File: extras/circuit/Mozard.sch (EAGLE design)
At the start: 43 parts, among them J4 Headphone/Line Out, U2 LM386

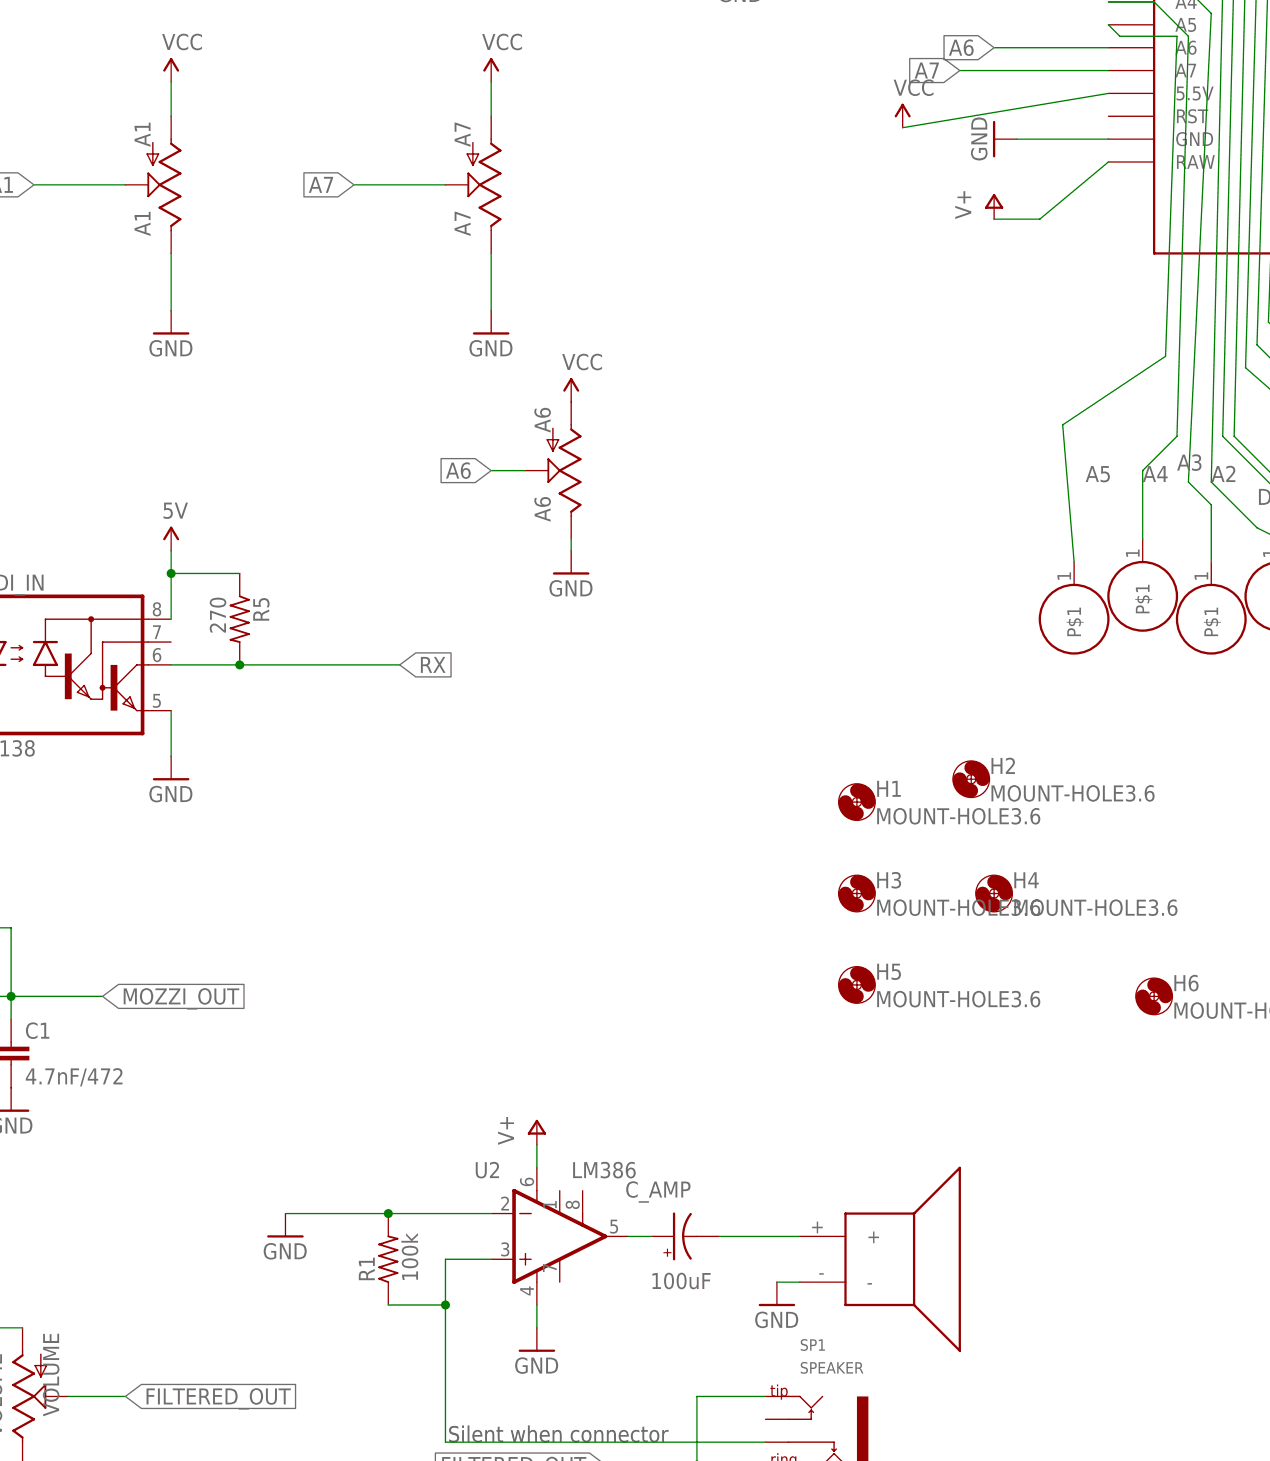
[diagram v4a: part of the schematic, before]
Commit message: Added MIDI
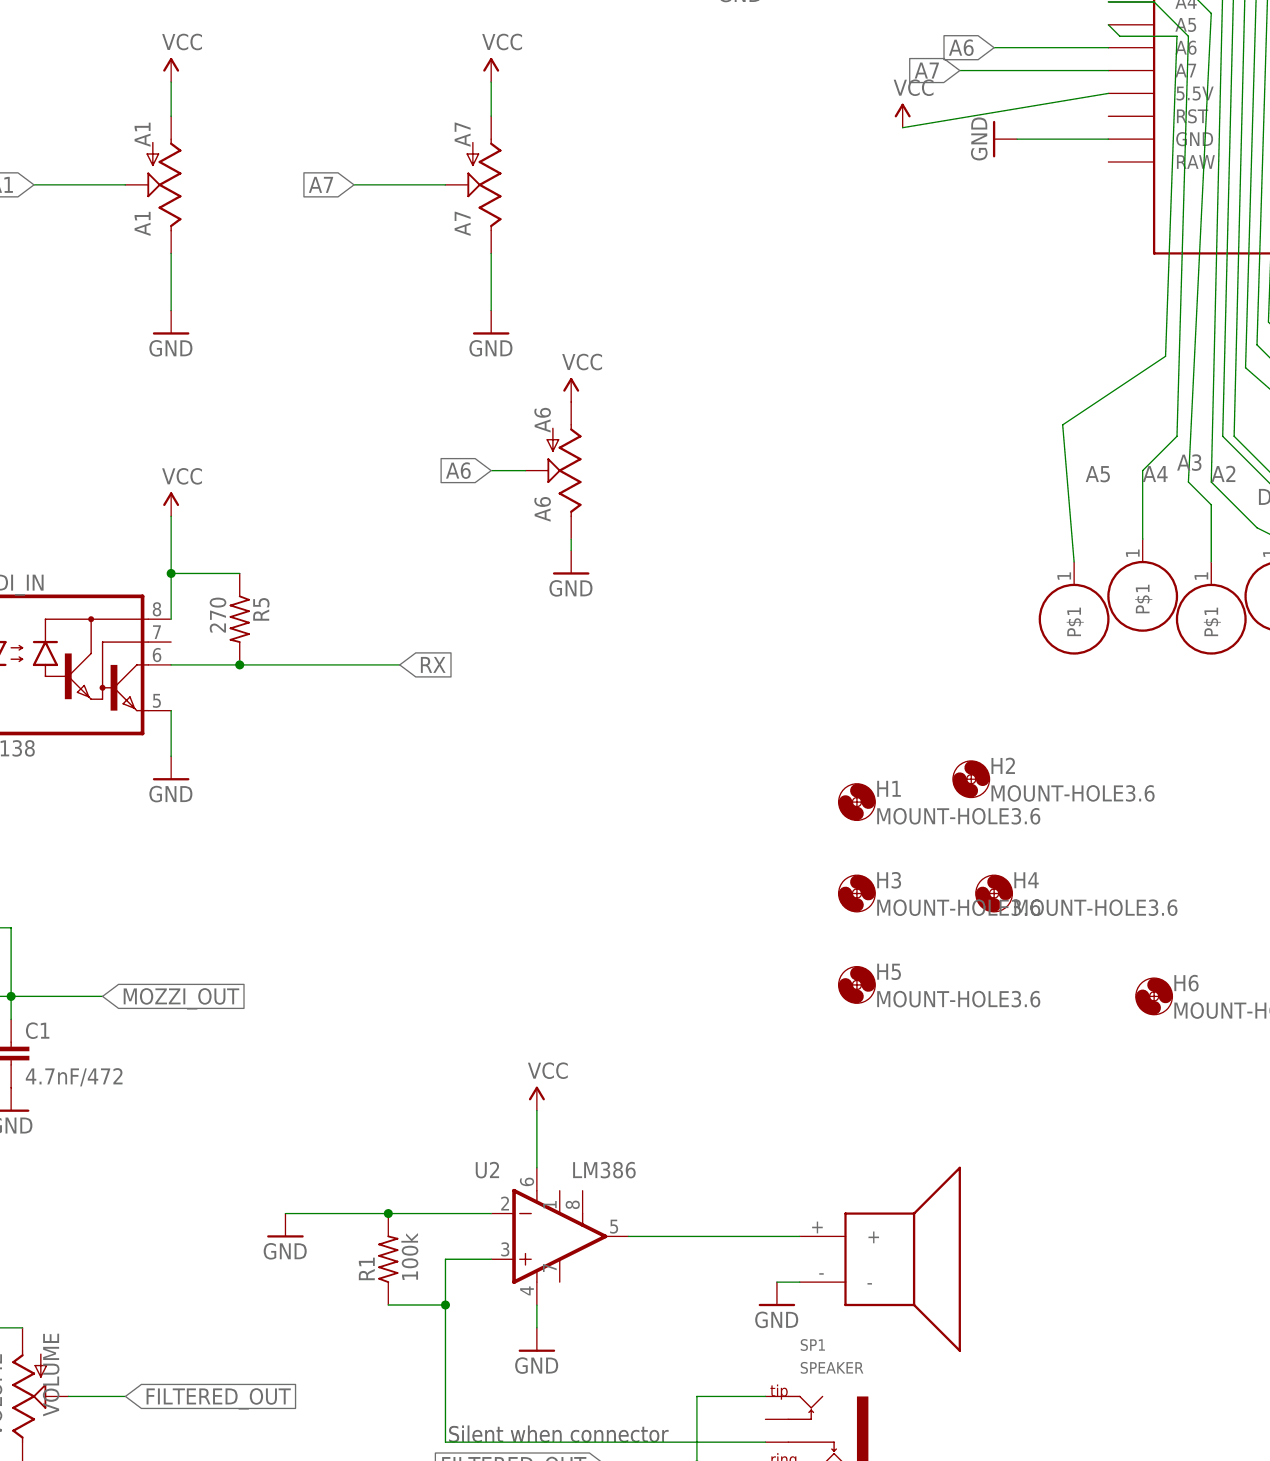
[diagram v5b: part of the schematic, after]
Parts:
- removed C_AMP: 100uF, TOF:CPOL-USE2.5-6
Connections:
- removed net 5V: MIDI_IN.VCC, R5.1
- removed net N$7: C_AMP.+, U2.OUT
- removed net V+: U$1.RAW, U2.V+
- net N$1: now also U2.OUT; no longer C_AMP.-
- net VCC: now also MIDI_IN.VCC, R5.1, U2.V+
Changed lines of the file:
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@@
 <?xml version="1.0" encoding="utf-8"?>
 <!DOCTYPE eagle SYSTEM "eagle.dtd">
-<eagle version="9.4.2">
+<eagle version="9.3.1">
 <drawing>
 <settings>
@@
 <part name="GND8" library="SparkFun-Aesthetics" deviceset="GND" device=""/>
 <part name="SUPPLY1" library="SparkFun-Aesthetics" deviceset="VCC" device=""/>
-<part name="P+2" library="supply1" library_urn="urn:adsk.eagle:library:371" deviceset="V+" device=""/>
 <part name="H1" library="holes" library_urn="urn:adsk.eagle:library:237" deviceset="MOUNT-HOLE" device="3.6" package3d_urn="urn:adsk.eagle:package:14272/1"/>
 <part name="H2" library="holes" library_urn="urn:adsk.eagle:library:237" deviceset="MOUNT-HOLE" device="3.6" package3d_urn="urn:adsk.eagle:package:14272/1"/>
@@
 <part name="GND14" library="SparkFun-Aesthetics" deviceset="GND" device=""/>
 <part name="U2" library="Mitch-parts" deviceset="LM386" device=""/>
-<part name="C_AMP" library="TOF" deviceset="CPOL-US" device="E2.5-6" package3d_urn="urn:adsk.eagle:package:23349/1" value="100uF"/>
-<part name="P+1" library="supply1" library_urn="urn:adsk.eagle:library:371" deviceset="V+" device=""/>
 <part name="U$1" library="TOF" deviceset="NANO" device=""/>
 <part name="C1" library="SparkFun-Capacitors" deviceset="0.1UF-50V-20%(PTH)" device="KIT-EZ" value="4.7nF/472"/>
@@
 <part name="GND29" library="SparkFun-Aesthetics" deviceset="GND" device=""/>
 <part name="R5" library="adafruit" deviceset="R-US_" device="0204/5" value="270"/>
-<part name="SUPPLY7" library="SparkFun-Aesthetics" deviceset="5V" device=""/>
 <part name="MIDI_IN1" library="TOF" deviceset="AUDIO-JACK" device="KIT"/>
 <part name="GND10" library="SparkFun-Aesthetics" deviceset="GND" device=""/>
@@
 <part name="U$14" library="TOF" deviceset="PCB-TOUCHPAD-1-PIN" device=""/>
 <part name="R1" library="adafruit" deviceset="R-US_" device="0204/7" value="100k"/>
+<part name="SUPPLY3" library="SparkFun-Aesthetics" deviceset="VCC" device=""/>
+<part name="SUPPLY7" library="SparkFun-Aesthetics" deviceset="VCC" device=""/>
 </parts>
 <sheets>
@@
 <attribute name="VALUE" x="156.464" y="167.386" size="1.778" layer="96"/>
 </instance>
-<instance part="P+2" gate="1" x="167.64" y="156.21" smashed="yes">
-<attribute name="VALUE" x="165.1" y="153.67" size="1.778" layer="96" rot="R90"/>
-</instance>
 <instance part="H1" gate="G$1" x="152.4" y="88.9" smashed="yes">
 <attribute name="NAME" x="154.432" y="89.4842" size="1.778" layer="95"/>
@@
 <attribute name="NAME" x="109.855" y="48.895" size="1.778" layer="95" rot="MR180"/>
 <attribute name="VALUE" x="120.65" y="48.895" size="1.778" layer="96" rot="MR180"/>
-</instance>
-<instance part="C_AMP" gate="G$1" x="132.08" y="40.64" smashed="yes" rot="R90">
-<attribute name="NAME" x="133.985" y="46.736" size="1.778" layer="95" rot="R180"/>
-<attribute name="VALUE" x="136.271" y="36.576" size="1.778" layer="96" rot="R180"/>
-</instance>
-<instance part="P+1" gate="1" x="116.84" y="53.34" smashed="yes">
-<attribute name="VALUE" x="114.3" y="50.8" size="1.778" layer="96" rot="R90"/>
 </instance>
 <instance part="U$1" gate="G$1" x="203.2" y="180.34" smashed="yes"/>
@@
 <attribute name="NAME" x="85.3186" y="111.76" size="1.778" layer="95" rot="R270"/>
 <attribute name="VALUE" x="80.518" y="111.76" size="1.778" layer="96" rot="R270"/>
-</instance>
-<instance part="SUPPLY7" gate="G$1" x="76.2" y="116.84" smashed="yes">
-<attribute name="VALUE" x="75.184" y="120.396" size="1.778" layer="96"/>
 </instance>
 <instance part="MIDI_IN1" gate="G$1" x="-22.86" y="101.6" smashed="yes" rot="MR0">
@@
 <attribute name="VALUE" x="103.632" y="35.56" size="1.778" layer="96" rot="R90"/>
 </instance>
+<instance part="SUPPLY3" gate="G$1" x="116.84" y="54.61" smashed="yes">
+<attribute name="VALUE" x="115.824" y="58.166" size="1.778" layer="96"/>
+</instance>
+<instance part="SUPPLY7" gate="G$1" x="76.2" y="120.65" smashed="yes">
+<attribute name="VALUE" x="75.184" y="124.206" size="1.778" layer="96"/>
+</instance>
 </instances>
 <busses>
@@
 <pinref part="JP5" gate="G$1" pin="1"/>
 <pinref part="SUPPLY5" gate="G$1" pin="VCC"/>
+</segment>
+<segment>
+<pinref part="SUPPLY3" gate="G$1" pin="VCC"/>
+<pinref part="U2" gate="G$1" pin="V+"/>
+<wire x1="116.84" y1="54.61" x2="116.84" y2="48.26" width="0.1524" layer="91"/>
+</segment>
+<segment>
+<pinref part="MIDI_IN" gate="G$1" pin="VCC"/>
+<pinref part="R5" gate="G$1" pin="1"/>
+<wire x1="76.2" y1="114.3" x2="76.2" y2="109.22" width="0.1524" layer="91"/>
+<wire x1="83.82" y1="114.3" x2="76.2" y2="114.3" width="0.1524" layer="91"/>
+<pinref part="SUPPLY7" gate="G$1" pin="VCC"/>
+<wire x1="76.2" y1="120.65" x2="76.2" y2="114.3" width="0.1524" layer="91"/>
+<junction x="76.2" y="114.3"/>
 </segment>
 </net>
@@
 </segment>
 </net>
-<net name="V+" class="0">
-<segment>
-<pinref part="P+2" gate="1" pin="V+"/>
-<wire x1="172.72" y1="153.67" x2="167.64" y2="153.67" width="0.1524" layer="91"/>
-<pinref part="U$1" gate="G$1" pin="RAW"/>
-<wire x1="172.72" y1="153.67" x2="180.34" y2="160.02" width="0.1524" layer="91"/>
-</segment>
-<segment>
-<wire x1="116.84" y1="48.26" x2="116.84" y2="50.8" width="0.1524" layer="91"/>
-<pinref part="U2" gate="G$1" pin="V+"/>
-<pinref part="P+1" gate="1" pin="V+"/>
-</segment>
-</net>
 <net name="A3" class="0">
 <segment>
@@
 <wire x1="191.77" y1="176.53" x2="189.23" y2="124.46" width="0.1524" layer="91"/>
 <pinref part="U$4" gate="G$1" pin="P$1"/>
-</segment>
-</net>
-<net name="N$7" class="0">
-<segment>
-<wire x1="127" y1="40.64" x2="129.54" y2="40.64" width="0.1524" layer="91"/>
-<pinref part="U2" gate="G$1" pin="OUT"/>
-<pinref part="C_AMP" gate="G$1" pin="+"/>
 </segment>
 </net>
@@
 <wire x1="100.33" y1="33.02" x2="106.68" y2="33.02" width="0.1524" layer="91"/>
 <junction x="106.68" y="33.02"/>
-</segment>
-</net>
-<net name="N$1" class="0">
-<segment>
-<pinref part="C_AMP" gate="G$1" pin="-"/>
-<wire x1="146.05" y1="40.64" x2="137.16" y2="40.64" width="0.1524" layer="91"/>
-<pinref part="SP1" gate="G$1" pin="+"/>
 </segment>
 </net>
@@
 </segment>
 </net>
-<net name="5V" class="0">
-<segment>
-<pinref part="MIDI_IN" gate="G$1" pin="VCC"/>
-<wire x1="76.2" y1="116.84" x2="76.2" y2="114.3" width="0.1524" layer="91"/>
-<pinref part="R5" gate="G$1" pin="1"/>
-<wire x1="76.2" y1="114.3" x2="76.2" y2="109.22" width="0.1524" layer="91"/>
-<wire x1="83.82" y1="114.3" x2="76.2" y2="114.3" width="0.1524" layer="91"/>
-<junction x="76.2" y="114.3"/>
-<pinref part="SUPPLY7" gate="G$1" pin="5V"/>
-</segment>
-</net>
 <net name="M5" class="0">
 <segment>
@@
 <wire x1="-2.54" y1="99.06" x2="27.94" y2="104.14" width="0.1524" layer="91"/>
 <label x="-14.986" y="99.822" size="1.778" layer="95"/>
+</segment>
+</net>
+<net name="N$1" class="0">
+<segment>
+<pinref part="U2" gate="G$1" pin="OUT"/>
+<pinref part="SP1" gate="G$1" pin="+"/>
+<wire x1="127" y1="40.64" x2="146.05" y2="40.64" width="0.1524" layer="91"/>
 </segment>
 </net>
@@
 packages will not be understood (or retained) with this version.
 </note>
-<note version="8.4" severity="warning">
-Since Version 8.4, EAGLE supports properties for SPICE simulation.
-Probes in schematics and SPICE mapping objects found in parts and library devices
-will not be understood with this version. Update EAGLE to the latest version
-for full support of SPICE simulation.
-</note>
 </compatibility>
